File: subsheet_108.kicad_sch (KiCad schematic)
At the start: 16 parts

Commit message: update comments in cartridge
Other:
- title: Conversion du Thomson MO5 — Unité centrale v1 -> Conversion du Thomson MO5 — Unité centrale v2
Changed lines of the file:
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@@
   (paper "A4" portrait)
   (title_block
-    (title "Conversion du Thomson MO5 — Unité centrale v1")
-    (date "2024-12-30")
-    (rev "v1.0.0-rc2")
+    (title "Conversion du Thomson MO5 — Unité centrale v2")
+    (date "2025-02-08")
+    (rev "v2.0.0-alpha")
     (comment 1 "http://github.com/sporniket/kicad-conversions--thomson-mo5--v1")
-    (comment 3 "Gate Array Motorola MCA 1300 ALS")
-    (comment 4 "Reference : POP5001 501994-01")
+    (comment 3 "Gate Array EFCIS")
   )
   (junction (at 109.22 68.58) (diameter 0) (color 0 0 0 0)

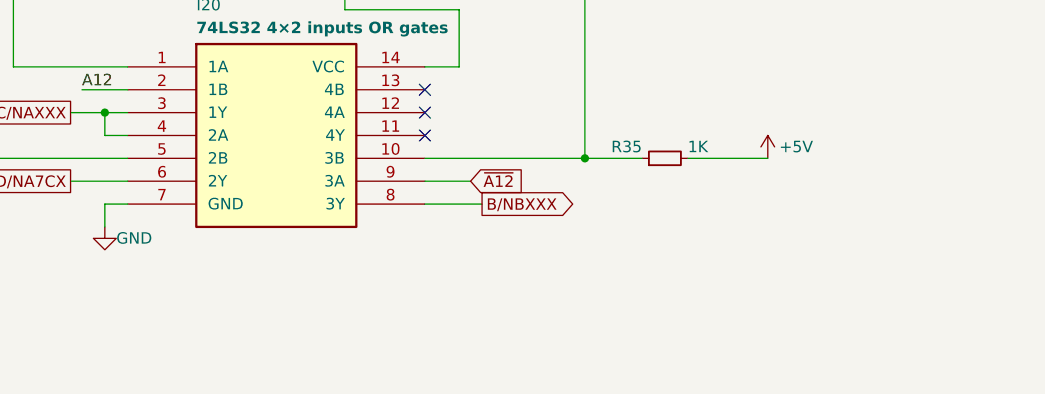
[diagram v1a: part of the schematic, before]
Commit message: Resolves #14 : [ga efcis] J01 and J02
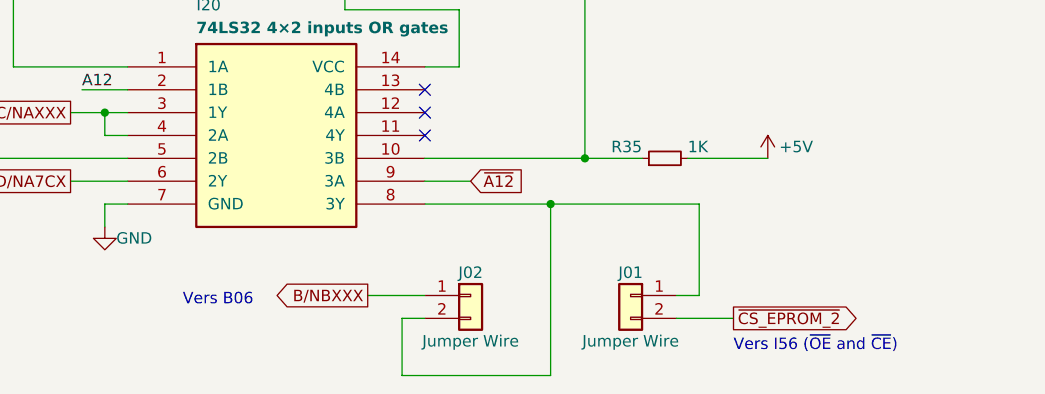
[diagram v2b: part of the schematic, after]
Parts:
- added J01, J02: Jumper Wire, symbol Connector_Generic:Conn_01x02
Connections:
- net B/NBXXX: now also J02.1 (Pin_1); no longer I20.8 (3Y)
- new net: I20.8 (3Y), J01.1 (Pin_1), J02.2 (Pin_2)
- new net ~{CS_EPROM_2}: J01.2 (Pin_2)
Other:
- note added: "Vers B06"
- note added: "Vers I56 (~{OE} and ~{CE})"
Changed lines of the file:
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@@
   (junction (at 130.81 205.74) (diameter 0) (color 0 0 0 0)
+  )
+  (junction (at 153.67 231.14) (diameter 0) (color 0 0 0 0)
   )
   (junction (at 104.14 220.98) (diameter 0) (color 0 0 0 0)
@@
     (stroke (width 0) (type default))
   )
+  (wire (pts (xy 137.16 243.84) (xy 137.16 250.19))
+    (stroke (width 0) (type default))
+  )
   (wire (pts (xy 83.82 157.48) (xy 86.36 157.48))
     (stroke (width 0) (type default))
@@
     (stroke (width 0) (type default))
   )
+  (wire (pts (xy 167.64 243.84) (xy 173.99 243.84))
+    (stroke (width 0) (type default))
+  )
   (wire (pts (xy 144.78 96.52) (xy 153.67 96.52))
     (stroke (width 0) (type default))
@@
     (stroke (width 0) (type default))
   )
+  (wire (pts (xy 153.67 250.19) (xy 153.67 231.14))
+    (stroke (width 0) (type default))
+  )
   (wire (pts (xy 116.84 129.54) (xy 124.46 129.54))
     (stroke (width 0) (type default))
@@
     (stroke (width 0) (type default))
   )
-  (wire (pts (xy 139.7 231.14) (xy 146.05 231.14))
+  (wire (pts (xy 139.7 231.14) (xy 153.67 231.14))
     (stroke (width 0) (type default))
   )
@@
     (stroke (width 0) (type default))
   )
+  (wire (pts (xy 139.7 243.84) (xy 137.16 243.84))
+    (stroke (width 0) (type default))
+  )
   (wire (pts (xy 182.88 38.1) (xy 182.88 111.76))
     (stroke (width 0) (type default))
@@
     (stroke (width 0) (type default))
   )
+  (wire (pts (xy 170.18 231.14) (xy 170.18 241.3))
+    (stroke (width 0) (type default))
+  )
   (wire (pts (xy 106.68 226.06) (xy 71.12 226.06))
     (stroke (width 0) (type default))
@@
     (stroke (width 0) (type default))
   )
+  (wire (pts (xy 133.35 241.3) (xy 139.7 241.3))
+    (stroke (width 0) (type default))
+  )
   (wire (pts (xy 93.98 58.42) (xy 101.6 58.42))
     (stroke (width 0) (type default))
@@
     (stroke (width 0) (type default))
   )
+  (wire (pts (xy 137.16 250.19) (xy 153.67 250.19))
+    (stroke (width 0) (type default))
+  )
   (wire (pts (xy 52.07 147.32) (xy 52.07 146.05))
     (stroke (width 0) (type default))
@@
     (stroke (width 0) (type default))
   )
+  (wire (pts (xy 153.67 231.14) (xy 170.18 231.14))
+    (stroke (width 0) (type default))
+  )
   (wire (pts (xy 55.88 58.42) (xy 60.96 58.42))
     (stroke (width 0) (type default))
@@
     (stroke (width 0) (type default))
   )
+  (wire (pts (xy 170.18 241.3) (xy 167.64 241.3))
+    (stroke (width 0) (type default))
+  )
   (wire (pts (xy 38.1 71.12) (xy 60.96 71.12))
     (stroke (width 0) (type default))
@@
   (wire (pts (xy 93.98 68.58) (xy 109.22 68.58))
     (stroke (width 0) (type default))
+  )
+  (text "Vers I56 (~{OE} and ~{CE})" (at 173.99 247.65 0)
+    (effects (font (size 1.27 1.27)) (justify left bottom))
+  )
+  (text "Vers B06" (at 120.65 242.57 0)
+    (effects (font (size 1.27 1.27)) (justify right bottom))
   )
   (text "Vers I04" (at 36.83 148.59 0)
@@
     )
   )
-  (global_label "B{slash}NBXXX" (shape output) (at 146.05 231.14 0) (fields_autoplaced)
-    (effects (font (size 1.27 1.27)) (justify left))
-    (property "Intersheetrefs" "${INTERSHEET_REFS}" (at 157.2926 231.0606 0)
-      (effects (font (size 1.27 1.27)) (justify left) hide)
+  (global_label "B{slash}NBXXX" (shape output) (at 133.35 241.3 180) (fields_autoplaced)
+    (effects (font (size 1.27 1.27)) (justify right))
+    (property "Intersheetrefs" "${INTERSHEET_REFS}" (at 121.5353 241.3 0)
+      (effects (font (size 1.27 1.27)) (justify right) hide)
     )
   )
@@
     (property "Intersheetrefs" "${INTERSHEET_REFS}" (at 54.3136 170.1006 0)
       (effects (font (size 1.27 1.27)) (justify right) hide)
+    )
+  )
+  (global_label "~{CS_EPROM_2}" (shape output) (at 173.99 243.84 0) (fields_autoplaced)
+    (effects (font (size 1.27 1.27)) (justify left))
+    (property "Intersheetrefs" "${INTERSHEET_REFS}" (at 189.0703 243.84 0)
+      (effects (font (size 1.27 1.27)) (justify left) hide)
     )
   )
@@
         (path "/e63e39d7-6ac0-4ffd-8aa3-1841a4541b55/5f0e2042-532a-4df5-a841-fef7a1a0ec91"
           (reference "#PWR0120") (unit 1)
+        )
+      )
+    )
+  )
+  (symbol (lib_id "Connector_Generic:Conn_01x02") (at 162.56 241.3 0) (mirror y) (unit 1)
+    (in_bom yes) (on_board yes) (dnp no)
+    (property "Reference" "J01" (at 162.56 238.76 0)
+      (effects (font (size 1.27 1.27)))
+    )
+    (property "Value" "Jumper Wire" (at 162.56 246.38 0)
+      (effects (font (size 1.27 1.27)))
+    )
+    (property "Footprint" "" (at 162.56 241.3 0)
+      (effects (font (size 1.27 1.27)) hide)
+    )
+    (property "Datasheet" "~" (at 162.56 241.3 0)
+      (effects (font (size 1.27 1.27)) hide)
+    )
+    (pin "2")
+    (pin "1")
+    (instances
+      (project "UC-50-001"
+        (path "/e63e39d7-6ac0-4ffd-8aa3-1841a4541b55/5f0e2042-532a-4df5-a841-fef7a1a0ec91"
+          (reference "J01") (unit 1)
         )
       )
@@
         )
       )
+    )
+  )
+  (symbol (lib_id "Connector_Generic:Conn_01x02") (at 144.78 241.3 0) (unit 1)
+    (in_bom yes) (on_board yes) (dnp no)
+    (property "Reference" "J02" (at 144.78 238.76 0)
+      (effects (font (size 1.27 1.27)))
+    )
+    (property "Value" "Jumper Wire" (at 144.78 246.38 0)
+      (effects (font (size 1.27 1.27)))
+    )
+    (property "Footprint" "" (at 144.78 241.3 0)
+      (effects (font (size 1.27 1.27)) hide)
+    )
+    (property "Datasheet" "~" (at 144.78 241.3 0)
+      (effects (font (size 1.27 1.27)) hide)
+    )
+    (pin "2")
+    (pin "1")
+    (instances
+      (project "UC-50-001"
+        (path "/e63e39d7-6ac0-4ffd-8aa3-1841a4541b55/5f0e2042-532a-4df5-a841-fef7a1a0ec91"
+          (reference "J02") (unit 1)
+        )
+      )

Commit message: fixed some naming, assigned footprints to symbols without one, added them to pcb
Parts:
- J01, J02: footprint (none) -> thomson-moto-passives:Passive_THT_jumper_wire_W2.54mm_L10.16mm
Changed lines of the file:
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@@
       (effects (font (size 1.27 1.27)))
     )
-    (property "Footprint" "" (at 162.56 241.3 0)
+    (property "Footprint" "thomson-moto-passives:Passive_THT_jumper_wire_W2.54mm_L10.16mm" (at 162.56 241.3 0)
       (effects (font (size 1.27 1.27)) hide)
     )
@@
       (effects (font (size 1.27 1.27)))
     )
-    (property "Footprint" "" (at 144.78 241.3 0)
+    (property "Footprint" "thomson-moto-passives:Passive_THT_jumper_wire_W2.54mm_L10.16mm" (at 144.78 241.3 0)
       (effects (font (size 1.27 1.27)) hide)
     )

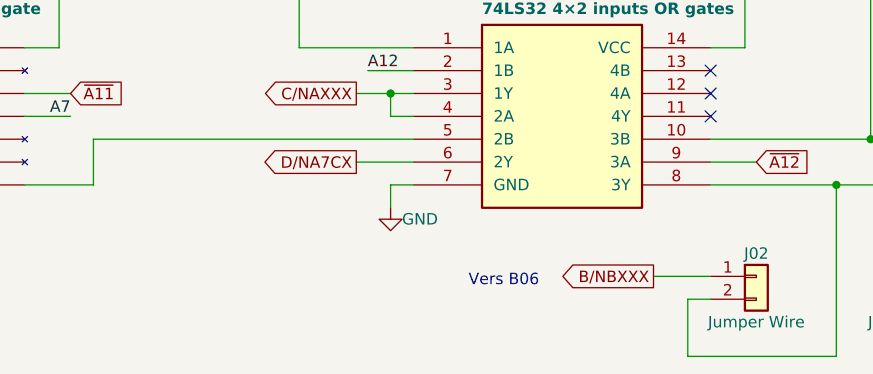
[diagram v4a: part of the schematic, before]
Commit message: Fixed : missing R95, 4K7 pull-up on NBxxx signal
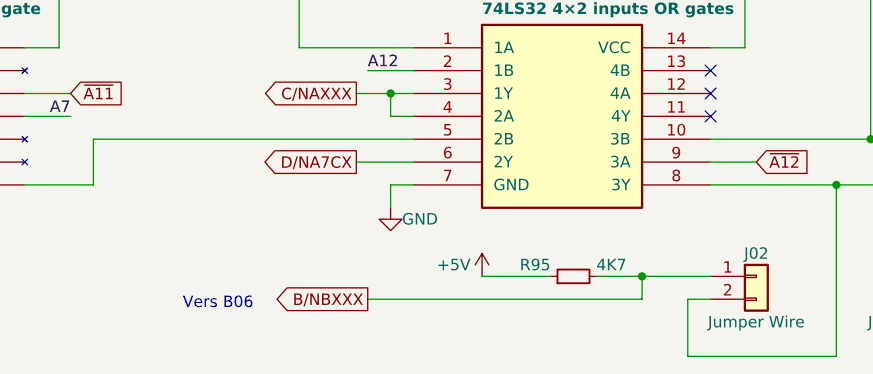
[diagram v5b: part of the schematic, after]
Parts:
- added R95: 4K7, commons-passives_THT:Passive_THT_resistor_EU_W2.54mm_L12.70mm, symbol Device:R_Small
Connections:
- net +5V: now also R95.1
- net B/NBXXX: now also R95.2
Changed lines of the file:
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@@
   (junction (at 157.48 226.06) (diameter 0) (color 0 0 0 0)
+  )
+  (junction (at 132.08 241.3) (diameter 0) (color 0 0 0 0)
   )
   (junction (at 134.62 129.54) (diameter 0) (color 0 0 0 0)
@@
     (stroke (width 0) (type default))
   )
+  (wire (pts (xy 127 241.3) (xy 132.08 241.3))
+    (stroke (width 0) (type default))
+  )
   (wire (pts (xy 135.89 86.36) (xy 143.51 86.36))
     (stroke (width 0) (type default))
@@
     (stroke (width 0) (type default))
   )
+  (wire (pts (xy 114.3 241.3) (xy 121.92 241.3))
+    (stroke (width 0) (type default))
+  )
   (wire (pts (xy 38.1 38.1) (xy 38.1 68.58))
     (stroke (width 0) (type default))
@@
     (stroke (width 0) (type default))
   )
-  (wire (pts (xy 133.35 241.3) (xy 139.7 241.3))
+  (wire (pts (xy 101.6 243.84) (xy 132.08 243.84))
     (stroke (width 0) (type default))
   )
@@
     (stroke (width 0) (type default))
   )
+  (wire (pts (xy 132.08 243.84) (xy 132.08 241.3))
+    (stroke (width 0) (type default))
+  )
   (wire (pts (xy 104.14 220.98) (xy 106.68 220.98))
     (stroke (width 0) (type default))
@@
   )
   (wire (pts (xy 63.5 231.14) (xy 71.12 231.14))
+    (stroke (width 0) (type default))
+  )
+  (wire (pts (xy 132.08 241.3) (xy 139.7 241.3))
     (stroke (width 0) (type default))
   )
@@
     (effects (font (size 1.27 1.27)) (justify left bottom))
   )
-  (text "Vers B06" (at 120.65 242.57 0)
+  (text "Vers B06" (at 88.9 245.11 0)
     (effects (font (size 1.27 1.27)) (justify right bottom))
   )
@@
     )
   )
-  (global_label "B{slash}NBXXX" (shape output) (at 133.35 241.3 180) (fields_autoplaced)
+  (global_label "B{slash}NBXXX" (shape output) (at 101.6 243.84 180) (fields_autoplaced)
     (effects (font (size 1.27 1.27)) (justify right))
-    (property "Intersheetrefs" "${INTERSHEET_REFS}" (at 121.5353 241.3 0)
+    (property "Intersheetrefs" "${INTERSHEET_REFS}" (at 89.7853 243.84 0)
       (effects (font (size 1.27 1.27)) (justify right) hide)
     )
@@
     )
   )
+  (symbol (lib_id "power:+5V") (at 114.3 241.3 0) (unit 1)
+    (in_bom yes) (on_board yes) (dnp no)
+    (property "Reference" "#PWR030" (at 114.3 245.11 0)
+      (effects (font (size 1.27 1.27)) hide)
+    )
+    (property "Value" "+5V" (at 113.03 240.03 0)
+      (effects (font (size 1.27 1.27)) (justify right))
+    )
+    (property "Footprint" "" (at 114.3 241.3 0)
+      (effects (font (size 1.27 1.27)) hide)
+    )
+    (property "Datasheet" "" (at 114.3 241.3 0)
+      (effects (font (size 1.27 1.27)) hide)
+    )
+    (pin "1")
+    (instances
+      (project "UC-50-001"
+        (path "/e63e39d7-6ac0-4ffd-8aa3-1841a4541b55/5f0e2042-532a-4df5-a841-fef7a1a0ec91"
+          (reference "#PWR030") (unit 1)
+        )
+      )
+    )
+  )
   (symbol (lib_id "power:GND") (at 135.89 86.36 0) (unit 1)
     (in_bom yes) (on_board yes) (dnp no)
@@
         )
       )
+    )
+  )
+  (symbol (lib_id "Device:R_Small") (at 124.46 241.3 90) (unit 1)
+    (in_bom yes) (on_board yes) (dnp no)
+    (property "Reference" "R95" (at 121.92 240.03 90)
+      (effects (font (size 1.27 1.27)) (justify left))
+    )
+    (property "Value" "4K7" (at 127 240.03 90)
+      (effects (font (size 1.27 1.27)) (justify right))
+    )
+    (property "Footprint" "commons-passives_THT:Passive_THT_resistor_EU_W2.54mm_L12.70mm" (at 124.46 241.3 0)
+      (effects (font (size 1.27 1.27)) hide)
+    )
+    (property "Datasheet" "~" (at 124.46 241.3 0)
+      (effects (font (size 1.27 1.27)) hide)
+    )
+    (pin "1")
+    (pin "2")
+    (instances
+      (project "UC-50-001"
+        (path "/e63e39d7-6ac0-4ffd-8aa3-1841a4541b55/5f0e2042-532a-4df5-a841-fef7a1a0ec91"
+          (reference "R95") (unit 1)
+        )
+      )

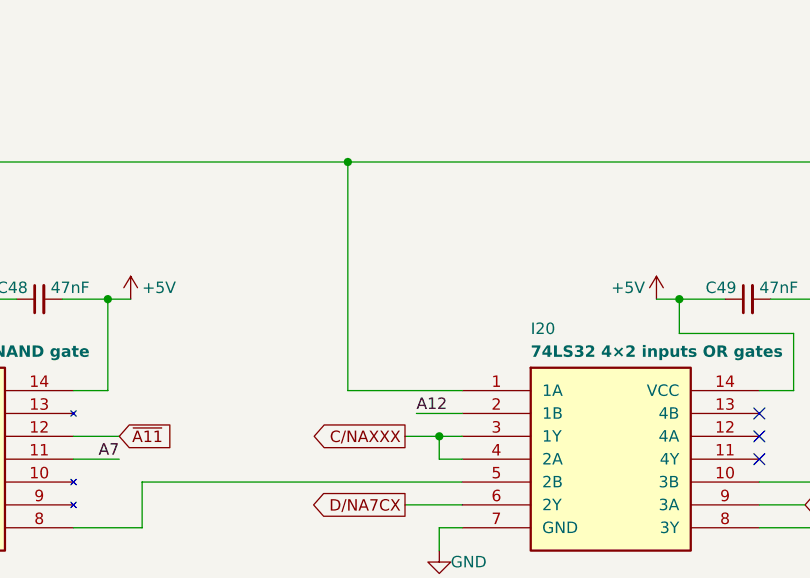
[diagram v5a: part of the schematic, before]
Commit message: Fixed I20 : exchanged pin 1 and 2
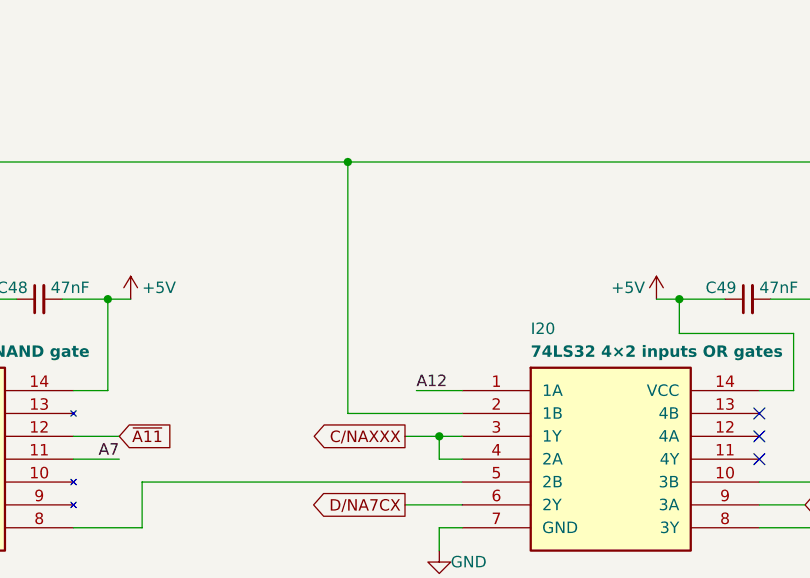
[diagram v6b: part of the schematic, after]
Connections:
- net A12: now also I20.1 (1A); no longer I20.2 (1B)
- net at I14.6 (1Y1), I20.10 (3B), R35.1: now also I20.2 (1B); no longer I20.1 (1A)
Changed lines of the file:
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@@
+    (stroke (width 0) (type default))
+  )
+  (wire (pts (xy 101.6 215.9) (xy 106.68 215.9))
     (stroke (width 0) (type default))
   )
@@
     (stroke (width 0) (type default))
   )
-  (wire (pts (xy 93.98 190.5) (xy 93.98 215.9))
+  (wire (pts (xy 93.98 190.5) (xy 93.98 218.44))
     (stroke (width 0) (type default))
   )
@@
     (stroke (width 0) (type default))
   )
-  (wire (pts (xy 93.98 215.9) (xy 106.68 215.9))
-    (stroke (width 0) (type default))
-  )
   (wire (pts (xy 119.38 154.94) (xy 123.19 154.94))
     (stroke (width 0) (type default))
@@
     (stroke (width 0) (type default))
   )
-  (wire (pts (xy 101.6 218.44) (xy 106.68 218.44))
+  (wire (pts (xy 93.98 218.44) (xy 106.68 218.44))
     (stroke (width 0) (type default))
   )
@@
     (effects (font (size 1.27 1.27)) (justify right bottom))
   )
-  (label "A12" (at 101.6 218.44 0) (fields_autoplaced)
-    (effects (font (size 1.27 1.27)) (justify left bottom))
-  )
+  (label "A12" (at 101.6 215.9 0) (fields_autoplaced)
+    (effects (font (size 1.27 1.27)) (justify left bottom))
+  )
